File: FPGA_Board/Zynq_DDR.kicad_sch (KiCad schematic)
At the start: 0 parts

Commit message: add FPGA,DDR, Decoupling capacitor symbols for power & ddr sheets. modify symbols pinout placement to clean up schematic
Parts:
- added U5: XC7Z010-2CLG400I, FPGA_BOARD:CLG400, symbol FPGA_Parts:CMP-0363-00008-3
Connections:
- new net DDR_DQ0: U5.C3 (PS_DDR_DQ0_502)
- new net DDR_DQ1: U5.B3 (PS_DDR_DQ1_502)
- new net DDR_DQ2: U5.A2 (PS_DDR_DQ2_502)

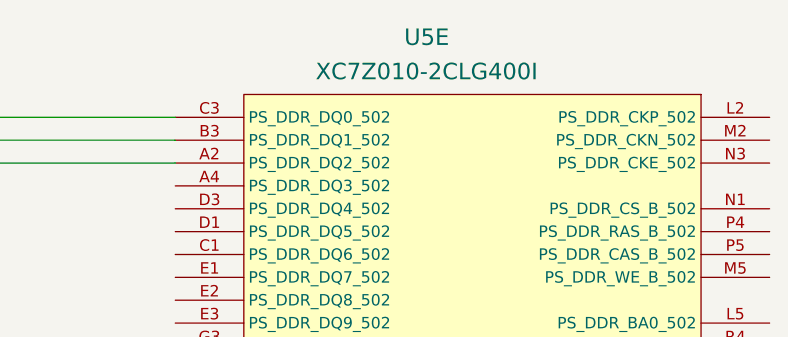
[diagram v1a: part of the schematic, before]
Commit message: Add DDR VTT power module, add Zynq power + decoupling, placed Zynq DDR
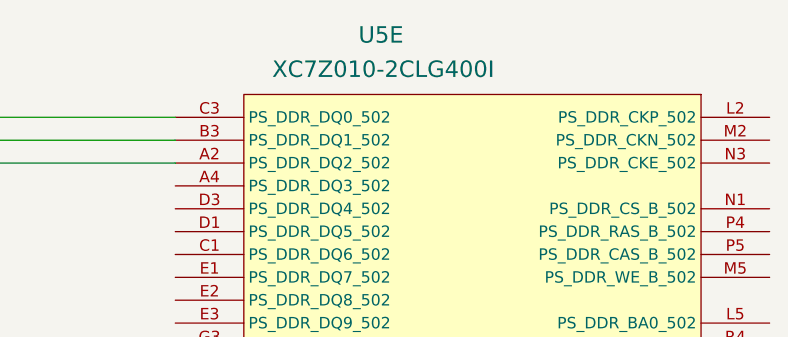
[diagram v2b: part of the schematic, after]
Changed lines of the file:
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@@
 		(fields_autoplaced yes)
 		(property "Reference" "U5"
-			(at 86.36 26.67 0)
+			(at 81.28 26.416 0)
 			(show_name no)
 			(do_not_autoplace no)
@@
 		)
 		(property "Value" "XC7Z010-2CLG400I"
-			(at 86.36 30.48 0)
+			(at 81.534 30.226 0)
 			(show_name no)
 			(do_not_autoplace no)
